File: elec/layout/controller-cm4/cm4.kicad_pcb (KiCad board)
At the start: 2 copper layers, 40 parts, among them U1 10nF ±10% 50V X7R, U10 12.4kΩ ±1% 62.5mW, U11 1nF ±10% 50V X7R, U12 220Ω ±1% 62.5mW, U13 1MΩ ±1% 62.5mW, U15 10pF ±5% 50V C0G, U16 10pF ±5% 50V C0G, U19 10nF ±10% 50V X7R, U2 220Ω ±1% 62.5mW, U20 6.8nF ±10% 50V X7R, U21 33Ω ±1% 62.5mW, U22 49.9Ω ±1% 62.5mW, U23 6.8nF ±10% 50V X7R, U24 33Ω ±1% 62.5mW, U25 49.9Ω ±1% 62.5mW, U26 4.7µF ±10% 10V X5R, U27 22nF ±10% 50V X7R, U28 10Ω ±1% 62.5mW, U29 33Ω ±1% 62.5mW, U3 10µF ±10% 25V X5R, U30 49.9Ω ±1% 62.5mW, U31 33Ω ±1% 62.5mW, U32 49.9Ω ±1% 62.5mW, U34 10µF ±10% 25V X5R, U35 10µF ±10% 25V X5R, U37 10kΩ ±1% 62.5mW, U39 100nF ±10% 16V X7R, U4 100nF ±10% 16V X7R, U41 10kΩ ±1% 62.5mW, U5 100nF ±10% 16V X7R, U6 100nF ±10% 16V X7R, U7 100nF ±10% 16V X7R, U8 100nF ±10% 16V X7R, U9 100nF ±10% 16V X7R

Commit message: rebuild all modules
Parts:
- removed U11: 1nF ±10% 50V X7R, atopile:C0805-3b2e55
- removed U12, U2: 220Ω ±1% 62.5mW, atopile:R0402-56259e
- removed U14: , lib:CRYSTAL-SMD_4P-L3.2-W2.5-BL
- removed U15, U16: 10pF ±5% 50V C0G, atopile:C0402-b3ef17
- removed U18: , lib:RJ45-TH_J1B1211CCD
- removed U19: 10nF ±10% 50V X7R, atopile:C0402-b3ef17
- removed U20, U23: 6.8nF ±10% 50V X7R, atopile:C0402-b3ef17
- removed U21, U29: 33Ω ±1% 62.5mW, atopile:R0402-56259e
- removed U25: 49.9Ω ±1% 62.5mW, atopile:R0402-56259e
- removed U26: 4.7µF ±10% 10V X5R, atopile:C0402-b3ef17
- removed U27: 22nF ±10% 50V X7R, atopile:C0402-b3ef17
- removed U28: 10Ω ±1% 62.5mW, atopile:R0402-56259e
- removed U3, U34, U35: 10µF ±10% 25V X5R, atopile:C0805-3b2e55
- removed U36, U40: , lib:KEY-SMD_4P-L4.2-W3.2-P2.20-LS4.6
- removed U39, U4, U5, U6, U7, U8, U9: 100nF ±10% 16V X7R, atopile:C0402-b3ef17
- removed U41: 10kΩ ±1% 62.5mW, atopile:R0402-56259e
- added CN1: , atopile:CONN-SMD_DF40C-100DS-0.4V-51-ceffa9, F.Cu at (20.0, -5.00)
- added CN2: , atopile:CONN-SMD_DF40C-100DS-0.4V-51-ceffa9, F.Cu at (90.0, -5.00)
- added D1: , atopile:LED0603-RD-YELLOW-5af84a, F.Cu at (80.0, -5.00)
- added D2: , atopile:LED0603-RD-c81ffb, F.Cu at (30.0, -5.00)
- added R1: 1kΩ ±1% 62.5mW, atopile:R0402-56259e, F.Cu at (40.0, -5.00)
- added R2: 1kΩ ±1% 62.5mW, atopile:R0402-56259e, F.Cu at (70.0, -5.00)
- added R3: 470Ω ±1% 100mW, atopile:R0603-ebcab9, F.Cu at (60.0, -5.00)
- added R4: 470Ω ±1% 100mW, atopile:R0603-ebcab9, F.Cu at (10.0, -5.00)
- added RJ1: , atopile:RJ45-TH_HR911130A-5845d4, F.Cu at (100.0, -5.00)
- U1: value 10nF ±10% 50V X7R -> (none); footprint atopile:C0402-b3ef17 -> atopile:SOT-23-5_L3.0-W1.7-P0.95-LS2.8-BR-9d80aa
- moved U1 142.5 mm to (50.0, -5.00), turned to 0 degrees
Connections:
- U1 pad 1: _1V2O -> N_C_
- U1 pad 2: gnd -> PWR_LED
- U10 pad 1: EXRES1 -> (no net)
- U10 pad 2: gnd -> (no net)
- U13 pad 1: xin -> (no net)
- U13 pad 2: xout -> (no net)
- U22 pad 1: RD_minus -> (no net)
- U22 pad 2: RCT -> (no net)
- U24 pad 2: ethernet-net-1 -> (no net)
- U30 pad 1: hv -> (no net)
- U30 pad 2: TD_minus -> (no net)
- U31 pad 1: TXP -> (no net)
- U32 pad 1: hv -> (no net)
- U33 pad 10: EXRES1 -> (no net)
- U33 pad 11: hv -> (no net)
- U33 pad 14: gnd -> (no net)
- U33 pad 15: hv -> (no net)
- U33 pad 16: gnd -> (no net)
- U33 pad 17: hv -> (no net)
- U33 pad 18: VBG -> (no net)
- U33 pad 19: gnd -> (no net)
- U33 pad 2: TXP -> (no net)
- U33 pad 20: TOCAP -> (no net)
- U33 pad 21: hv -> (no net)
- U33 pad 22: _1V2O -> (no net)
- U33 pad 24: SPDLED -> (no net)
- U33 pad 25: LINKLED -> (no net)
- U33 pad 26: DUPLED -> (no net)
- U33 pad 28: hv -> (no net)
- U33 pad 29: gnd -> (no net)
- U33 pad 3: gnd -> (no net)
- U33 pad 30: xin -> (no net)
- U33 pad 31: xout -> (no net)
- U33 pad 32: cs -> (no net)
- U33 pad 33: sck -> (no net)
- U33 pad 34: miso -> (no net)
- U33 pad 35: mosi -> (no net)
- U33 pad 36: interrupt -> (no net)
- U33 pad 37: reset -> (no net)
- U33 pad 4: hv -> (no net)
- U33 pad 43: hv -> (no net)
- U33 pad 44: hv -> (no net)
- U33 pad 45: hv -> (no net)
- U33 pad 48: gnd -> (no net)
- U33 pad 8: hv -> (no net)
- U33 pad 9: gnd -> (no net)
- U37 pad 1: hv -> (no net)
- U37 pad 2: in-1 -> (no net)
- U38 pad 1: gnd -> (no net)
- U38 pad 10: io17 -> (no net)
- U38 pad 12: io8 -> (no net)
- U38 pad 13: dm -> (no net)
- U38 pad 14: dp -> (no net)
- U38 pad 15: io3 -> (no net)
- U38 pad 17: io9 -> (no net)
- U38 pad 18: cs -> (no net)
- U38 pad 19: mosi -> (no net)
- U38 pad 2: hv -> (no net)
- U38 pad 20: sck -> (no net)
- U38 pad 21: miso -> (no net)
- U38 pad 22: io14 -> (no net)
- U38 pad 24: io47 -> (no net)
- U38 pad 25: io48 -> (no net)
- U38 pad 26: io45 -> (no net)
- U38 pad 27: in -> (no net)
- U38 pad 28: io35 -> (no net)
- U38 pad 3: in-1 -> (no net)
- U38 pad 30: io37 -> (no net)
- U38 pad 31: io38 -> (no net)
- U38 pad 32: tck -> (no net)
- U38 pad 33: tdo -> (no net)
- U38 pad 35: tms -> (no net)
- U38 pad 36: RXD0 -> (no net)
- U38 pad 37: TXD0 -> (no net)
- U38 pad 38: io2 -> (no net)
- U38 pad 39: io1 -> (no net)
- U38 pad 40: gnd -> (no net)
- U38 pad 41: gnd -> (no net)
- U38 pad 5: io5 -> (no net)
- U38 pad 7: line-1 -> (no net)
- U38 pad 8: io15 -> (no net)
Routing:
- net (no net): track 0.00 -> 406.6 mm, vias 0 -> 39
- net hv: track 51.9 -> 0.00 mm, vias 13 -> 0
- net gnd: track 45.3 -> 0.00 mm, vias 14 -> 0
- net RLED_minus: track 44.2 -> 0.00 mm
- net mosi: track 35.6 -> 0.00 mm, vias 2 -> 0
- net cs: track 32.4 -> 0.00 mm, vias 2 -> 0
- net in-1: track 32.2 -> 0.00 mm, vias 2 -> 0
- net sck: track 31.0 -> 0.00 mm, vias 2 -> 0
- net miso: track 30.3 -> 0.00 mm, vias 2 -> 0
- net CGND: track 27.5 -> 0.00 mm
- net xout: track 12.5 -> 0.00 mm
- net TD_minus: track 11.0 -> 0.00 mm, vias 2 -> 0
- net in: track 9.92 -> 0.00 mm
- net xin: track 9.44 -> 0.00 mm
- net TXP: track 8.75 -> 0.00 mm
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
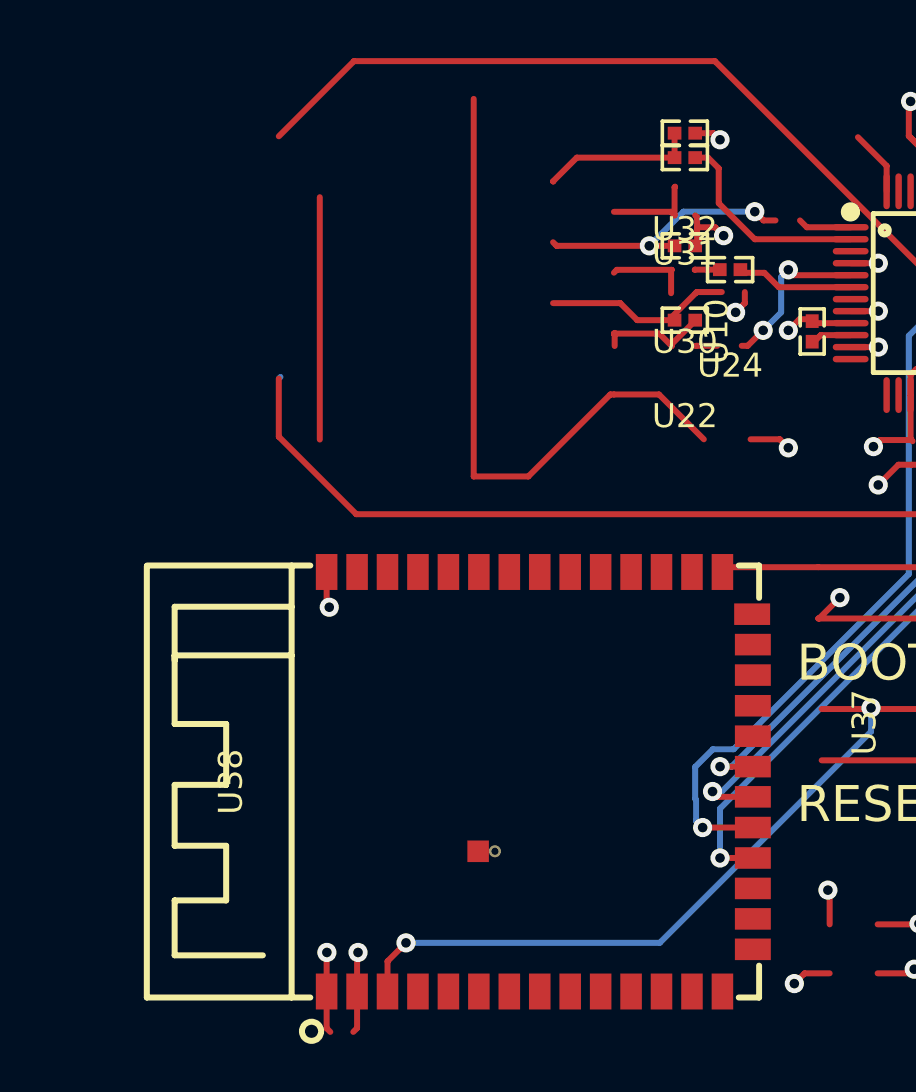
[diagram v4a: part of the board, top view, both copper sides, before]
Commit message: core layout, rebuild modules with compiler updates
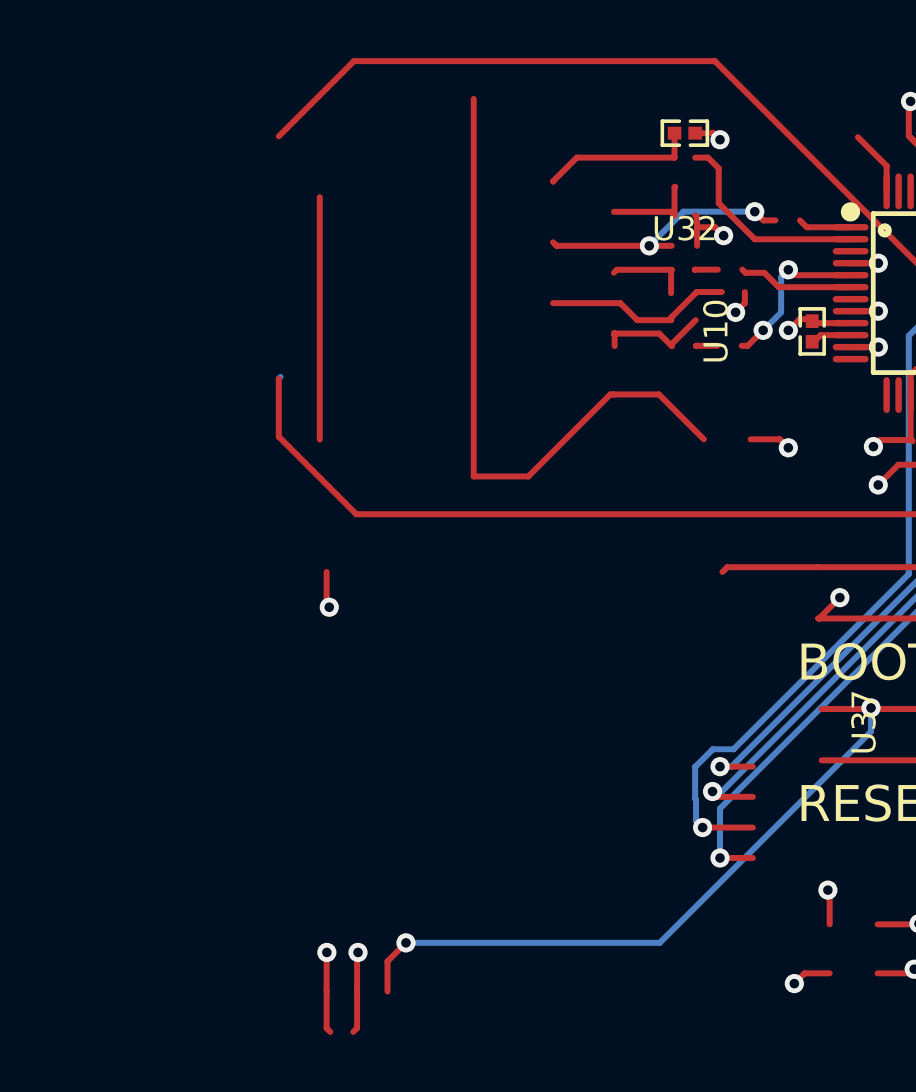
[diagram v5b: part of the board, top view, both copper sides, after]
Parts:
- removed U22, U30: 49.9Ω ±1% 62.5mW, atopile:R0402-56259e
- removed U24, U31: 33Ω ±1% 62.5mW, atopile:R0402-56259e
- removed U38: , lib:WIRELM-SMD_ESP32-S3-WROOM-1
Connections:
- net cm4-line-9 renamed pins[37]
- net cm4.hdi_b-pins[38] renamed pins[38]
- net pins[49] renamed cm4.hdi_b-pins[49]
- CN1 pad 1: GND -> (no net)
- CN1 pad 100: GND -> (no net)
- CN1 pad 11: GND -> (no net)
- CN1 pad 15: line-1 -> line
- CN1 pad 16: GND -> (no net)
- CN1 pad 17: line-2 -> line-1
- CN1 pad 20: cm4-line-5 -> cm4-line-4
- CN1 pad 21: GND -> (no net)
- CN1 pad 22: cm4-line-7 -> cm4-line-3
- CN1 pad 23: cm4-line-1 -> pins[45]
- CN1 pad 25: cm4-line-2 -> cm4-pins[49]
- CN1 pad 26: GND -> (no net)
- CN1 pad 27: line -> line-2
- CN1 pad 28: pins[55] -> cm4-line-7
- CN1 pad 29: cm4-line-4 -> pins[57]
- CN1 pad 30: GND -> (no net)
- CN1 pad 33: GND -> (no net)
- CN1 pad 37: GND -> (no net)
- CN1 pad 4: GND -> (no net)
- CN1 pad 49: GND -> (no net)
- CN1 pad 65: GND -> (no net)
- CN1 pad 68: GND -> (no net)
- CN1 pad 7: GND -> (no net)
- CN1 pad 71: GND -> (no net)
- CN1 pad 74: GND -> (no net)
- CN1 pad 75: pins[50] -> cm4-line-2
- CN1 pad 77: cm4-line-8 -> cm4-line
- CN1 pad 78: cm4-pins[44]-1 -> cm4-pins[44]
- CN1 pad 79: GND -> (no net)
- CN1 pad 81: cm4-pins[38] -> cm4-line-6
- CN1 pad 84: GND -> (no net)
- CN1 pad 85: cm4-line-6 -> cm4-line-1
- CN1 pad 87: cm4-line-3 -> cm4-line-5
- CN1 pad 89: GND -> (no net)
- CN1 pad 90: GND -> (no net)
- CN1 pad 94: GND -> (no net)
- CN1 pad 97: GND -> (no net)
- CN2 pad 10: GND -> (no net)
- CN2 pad 13: GND -> (no net)
- CN2 pad 16: GND -> (no net)
- CN2 pad 19: GND -> (no net)
- CN2 pad 22: GND -> (no net)
- CN2 pad 28: GND -> (no net)
- CN2 pad 31: GND -> (no net)
- CN2 pad 34: GND -> (no net)
- CN2 pad 37: GND -> (no net)
- CN2 pad 4: GND -> (no net)
- CN2 pad 40: GND -> (no net)
- CN2 pad 43: GND -> (no net)
- CN2 pad 46: GND -> (no net)
- CN2 pad 49: GND -> (no net)
- CN2 pad 52: GND -> (no net)
- CN2 pad 55: GND -> (no net)
- CN2 pad 58: GND -> (no net)
- CN2 pad 61: GND -> (no net)
- CN2 pad 64: GND -> (no net)
- CN2 pad 67: GND -> (no net)
- CN2 pad 7: GND -> (no net)
- CN2 pad 70: GND -> (no net)
- CN2 pad 73: GND -> (no net)
- CN2 pad 78: cm4-pins[44] -> cm4-pins[44]-1
- CN2 pad 82: GND -> (no net)
- CN2 pad 85: GND -> (no net)
- CN2 pad 88: GND -> (no net)
- CN2 pad 91: GND -> (no net)
- CN2 pad 94: GND -> (no net)
- CN2 pad 97: GND -> (no net)
- D1 pad 1: cm4-cathode-1 -> cm4-cathode
- D2 pad 1: cm4-cathode -> cm4-cathode-1
- R1 pad 1: cm4-cathode-1 -> cm4-cathode
- R2 pad 1: cm4-cathode -> cm4-cathode-1
- R2 pad 2: cm4-line -> Y
- R3 pad 2: rj45-anode -> rj45-anode-1
- R4 pad 2: rj45-anode-1 -> rj45-anode
- RJ1 pad 12: rj45-anode -> rj45-anode-1
- RJ1 pad 13: rj45-anode-1 -> rj45-anode
- RJ1 pad P1: rj45.connector-net-1 -> rj45.connector-net
- RJ1 pad P10: rj45.connector-net -> rj45.connector-net-1
- U1 pad 3: (no net) -> GND
- U1 pad 4: cm4-line -> Y
- U33 pad 1: TXN -> (no net)
- U33 pad 6: RXP -> (no net)
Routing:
- net (no net): track 406.6 -> 460.3 mm
- net LLED_minus: track 42.9 -> 0.00 mm
- net RXP: track 4.82 -> 0.00 mm
- net TCT: track 3.80 -> 0.00 mm
- net TXN: track 2.23 -> 0.00 mm
